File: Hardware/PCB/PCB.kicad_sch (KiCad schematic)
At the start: 0 parts

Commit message: added a lot of stuff, going to work on LCD + Touch next
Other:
- added sheet power (power.kicad_sch)
- added sheet relay_driver (relay_driver.kicad_sch)
- added sheet rtc (rtc.kicad_sch)
- added sheet serial_spi_lcd (serial_spi_lcd.kicad_sch)
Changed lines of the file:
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@@
 	(paper "A4")
 	(sheet
+		(at 36.83 154.94)
+		(size 19.685 13.97)
+		(fields_autoplaced yes)
+		(stroke
+			(width 0.1524)
+			(type solid)
+		)
+		(fill
+			(color 0 0 0 0.0000)
+		)
+		(property "Sheetname" "serial_spi_lcd"
+			(at 36.83 154.2284 0)
+			(effects
+				(font
+					(size 1.27 1.27)
+				)
+				(justify left bottom)
+			)
+		)
+		(property "Sheetfile" "serial_spi_lcd.kicad_sch"
+			(at 36.83 169.4946 0)
+			(effects
+				(font
+					(size 1.27 1.27)
+				)
+				(justify left top)
+			)
+		)
+		(instances
+			(project "PCB"
+				(path "/c3756407-a933-418d-a16a-ea4e5b091ef7"
+					(page "8")
+				)
+			)
+		)
+	)
+	(sheet
 		(at 209.55 102.87)
-		(size 35.56 24.13)
-		(fields_autoplaced yes)
-		(stroke
-			(width 0.1524)
-			(type solid)
-		)
-		(fill
-			(color 0 0 0 0.0000)
+		(size 26.67 29.845)
+		(fields_autoplaced yes)
+		(stroke
+			(width 0.1524)
+			(type solid)
+		)
+		(fill
+			(color 255 255 194 1.0000)
 		)
 		(property "Sheetname" "sensors"
@@
 		)
 		(property "Sheetfile" "sensors.kicad_sch"
-			(at 209.55 127.5846 0)
-			(effects
-				(font
-					(size 1.27 1.27)
-				)
-				(justify left top)
-			)
-		)
-		(instances
-			(project "PAC"
+			(at 209.55 133.2996 0)
+			(effects
+				(font
+					(size 1.27 1.27)
+				)
+				(justify left top)
+			)
+		)
+		(instances
+			(project "PCB"
 				(path "/c3756407-a933-418d-a16a-ea4e5b091ef7"
 					(page "3")
+				)
+			)
+		)
+	)
+	(sheet
+		(at 38.1 24.765)
+		(size 13.97 9.525)
+		(fields_autoplaced yes)
+		(stroke
+			(width 0.1524)
+			(type solid)
+		)
+		(fill
+			(color 72 72 72 1.0000)
+		)
+		(property "Sheetname" "power"
+			(at 38.1 24.0534 0)
+			(effects
+				(font
+					(size 1.27 1.27)
+				)
+				(justify left bottom)
+			)
+		)
+		(property "Sheetfile" "power.kicad_sch"
+			(at 38.1 34.8746 0)
+			(effects
+				(font
+					(size 1.27 1.27)
+				)
+				(justify left top)
+			)
+		)
+		(instances
+			(project "PCB"
+				(path "/c3756407-a933-418d-a16a-ea4e5b091ef7"
+					(page "5")
+				)
+			)
+		)
+	)
+	(sheet
+		(at 133.35 34.29)
+		(size 24.765 17.145)
+		(fields_autoplaced yes)
+		(stroke
+			(width 0.1524)
+			(type solid)
+		)
+		(fill
+			(color 255 255 194 1.0000)
+		)
+		(property "Sheetname" "relay_driver"
+			(at 133.35 33.5784 0)
+			(effects
+				(font
+					(size 1.27 1.27)
+				)
+				(justify left bottom)
+			)
+		)
+		(property "Sheetfile" "relay_driver.kicad_sch"
+			(at 133.35 52.0196 0)
+			(effects
+				(font
+					(size 1.27 1.27)
+				)
+				(justify left top)
+			)
+		)
+		(instances
+			(project "PCB"
+				(path "/c3756407-a933-418d-a16a-ea4e5b091ef7"
+					(page "6")
 				)
 			)
@@
 		)
 		(fill
-			(color 0 0 0 0.0000)
+			(color 255 255 194 1.0000)
 		)
 		(property "Sheetname" "motor_driver"
@@
 		)
 		(instances
-			(project "PAC"
+			(project "PCB"
 				(path "/c3756407-a933-418d-a16a-ea4e5b091ef7"
 					(page "2")
@@
 	)
 	(sheet
+		(at 28.575 89.535)
+		(size 19.05 18.415)
+		(fields_autoplaced yes)
+		(stroke
+			(width 0.1524)
+			(type solid)
+		)
+		(fill
+			(color 255 255 194 1.0000)
+		)
+		(property "Sheetname" "rtc"
+			(at 28.575 88.8234 0)
+			(effects
+				(font
+					(size 1.27 1.27)
+				)
+				(justify left bottom)
+			)
+		)
+		(property "Sheetfile" "rtc.kicad_sch"
+			(at 28.575 108.5346 0)
+			(effects
+				(font
+					(size 1.27 1.27)
+				)
+				(justify left top)
+			)
+		)
+		(instances
+			(project "PCB"
+				(path "/c3756407-a933-418d-a16a-ea4e5b091ef7"
+					(page "7")
+				)
+			)
+		)
+	)
+	(sheet
 		(at 91.44 57.15)
-		(size 26.67 26.67)
-		(fields_autoplaced yes)
-		(stroke
-			(width 0.1524)
-			(type solid)
-		)
-		(fill
-			(color 0 0 0 0.0000)
+		(size 21.59 65.405)
+		(fields_autoplaced yes)
+		(stroke
+			(width 0.1524)
+			(type solid)
+		)
+		(fill
+			(color 255 255 194 1.0000)
 		)
 		(property "Sheetname" "esp32"
@@
 		)
 		(property "Sheetfile" "esp32.kicad_sch"
-			(at 91.44 84.4046 0)
-			(effects
-				(font
-					(size 1.27 1.27)
-				)
-				(justify left top)
-			)
-		)
-		(instances
-			(project "PAC"
+			(at 91.44 123.1396 0)
+			(effects
+				(font
+					(size 1.27 1.27)
+				)
+				(justify left top)
+			)
+		)
+		(instances
+			(project "PCB"
 				(path "/c3756407-a933-418d-a16a-ea4e5b091ef7"
 					(page "4")

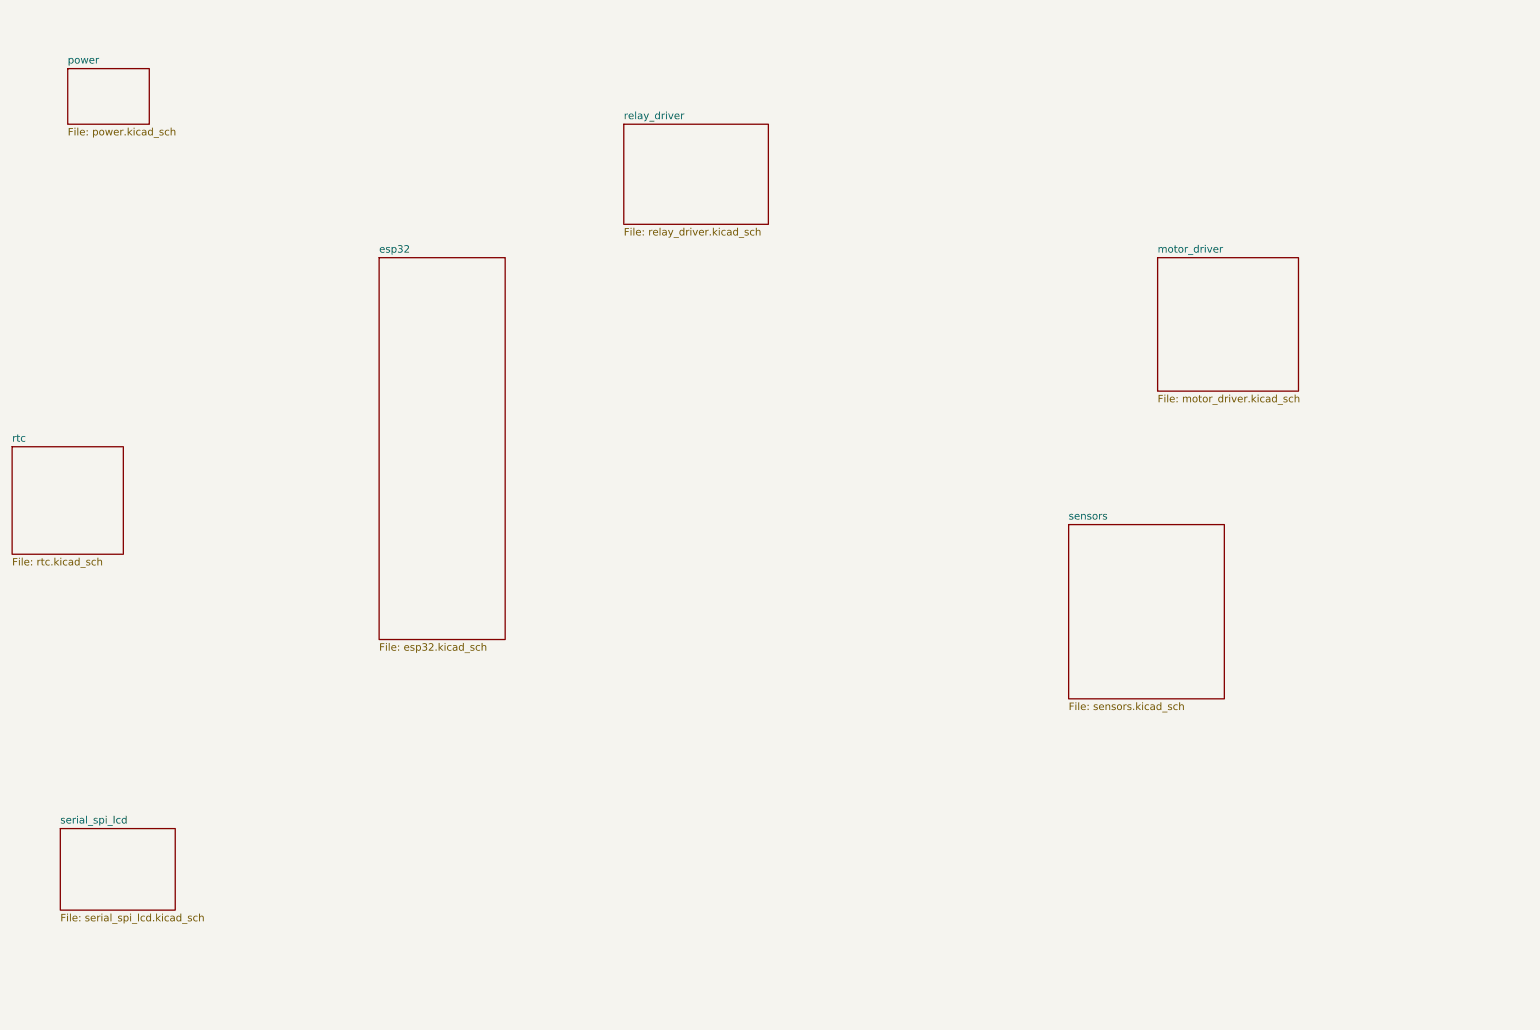
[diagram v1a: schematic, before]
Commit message: added symbol for LCD, working on adding PWM output terminal for brushless pump motors
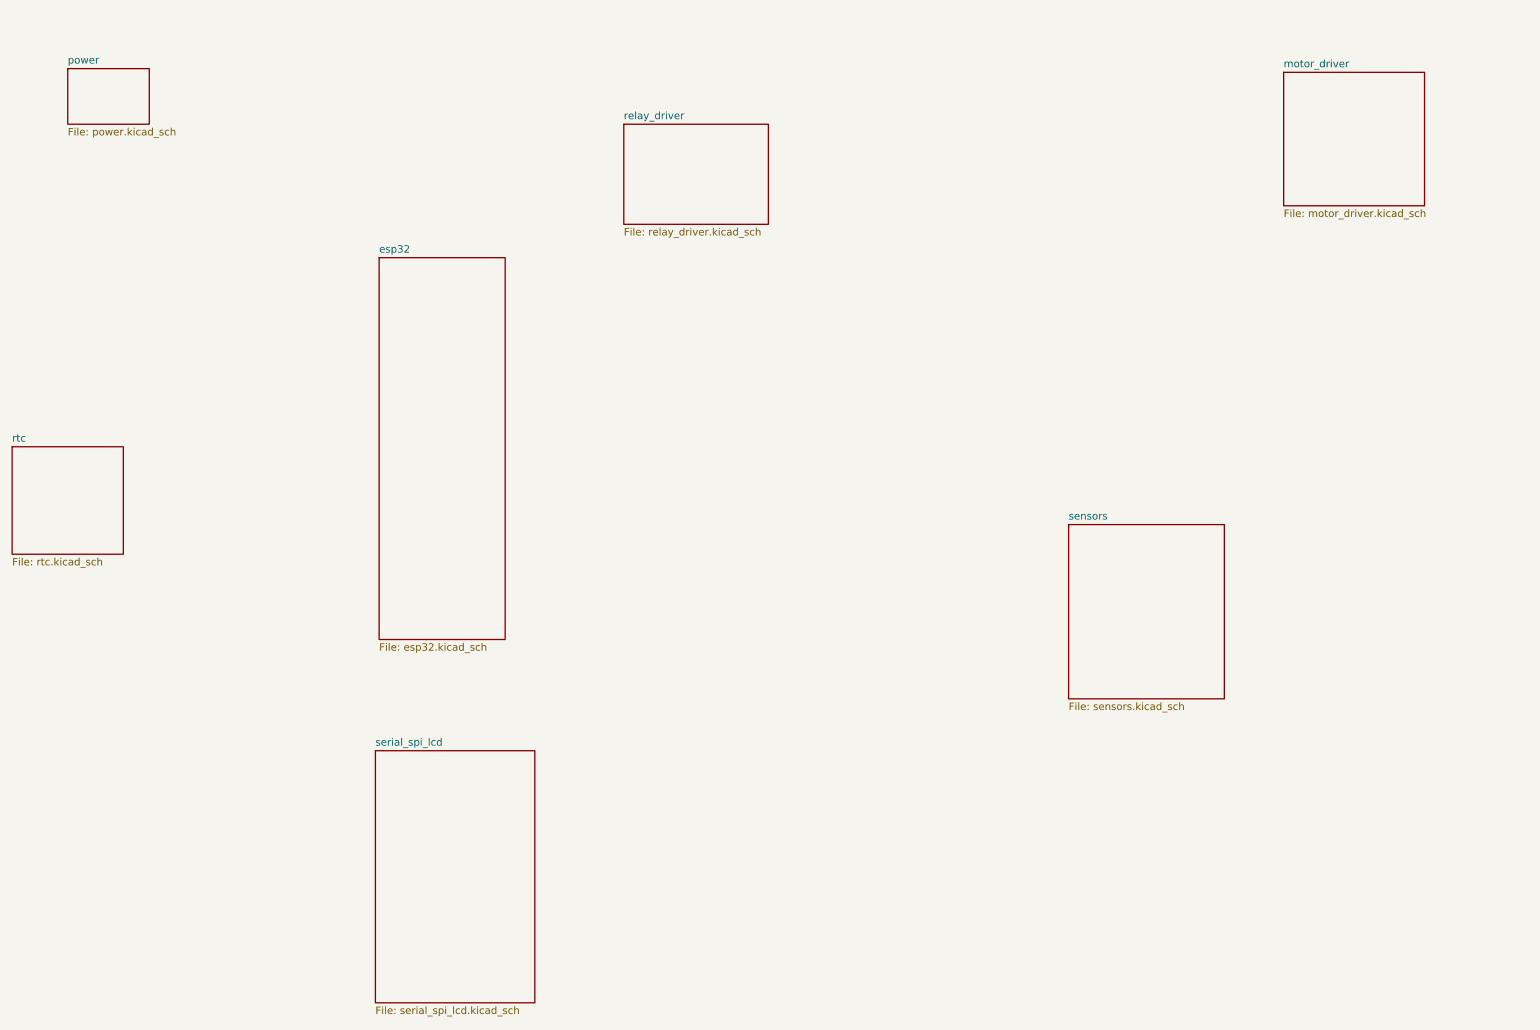
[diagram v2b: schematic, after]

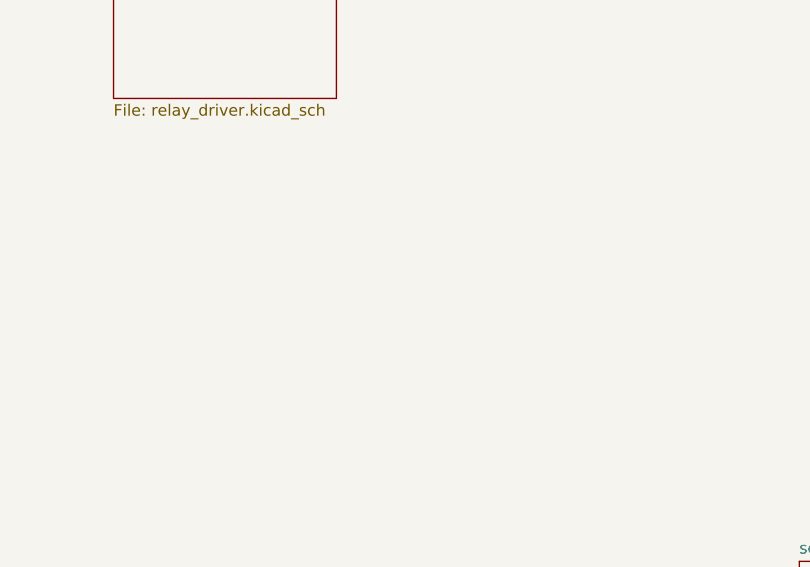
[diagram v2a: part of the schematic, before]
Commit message: switched to making buck converter to save costs and space, and to allow for LDO after 5.5V for better stability
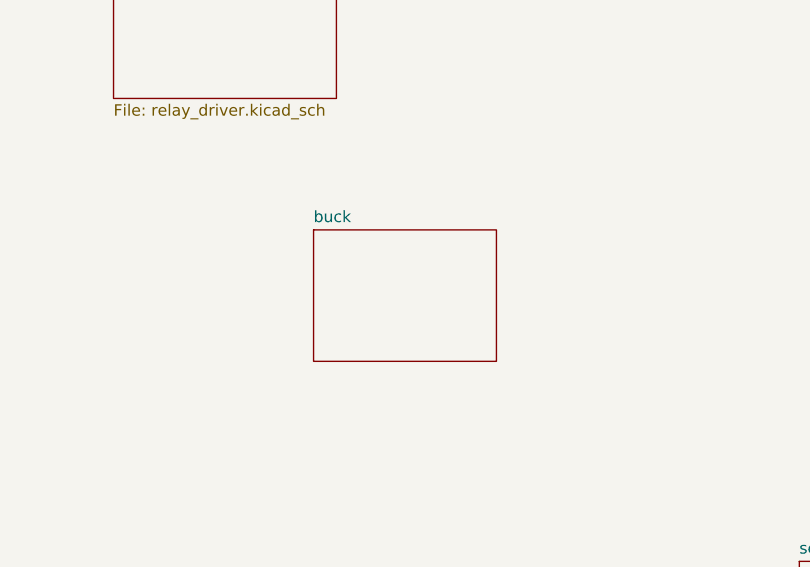
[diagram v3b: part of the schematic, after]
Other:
- added sheet buck (buck.kicad_sch)

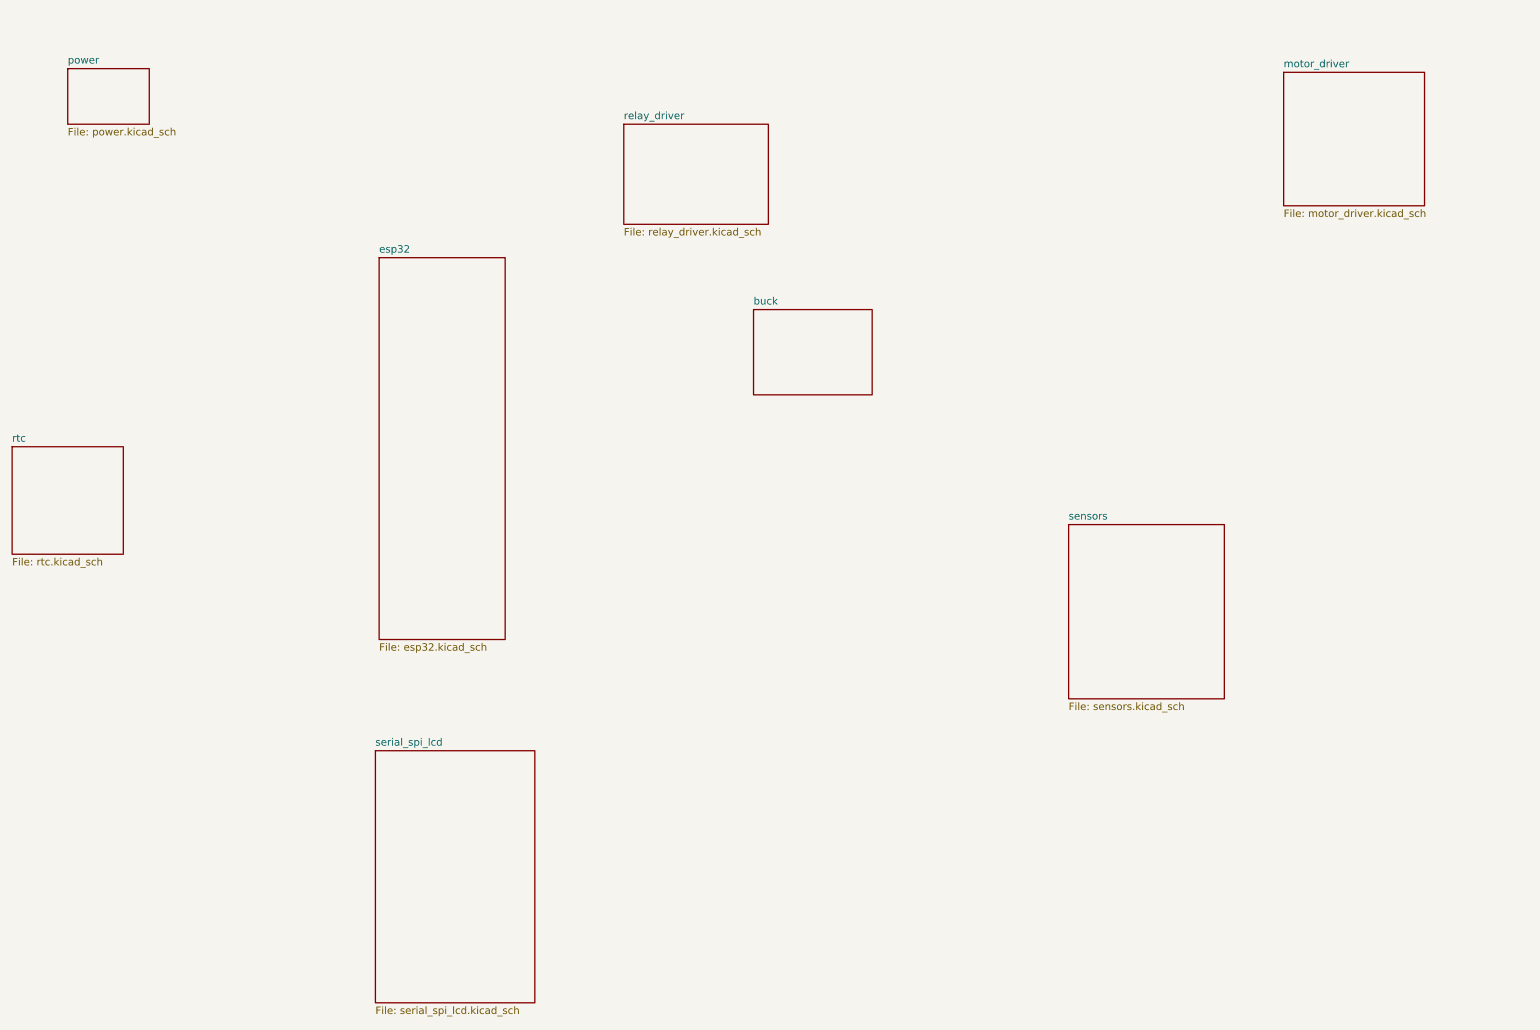
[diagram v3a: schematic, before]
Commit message: swapped to be better precision resistors for feedback on buck and votlage reference for ADCs
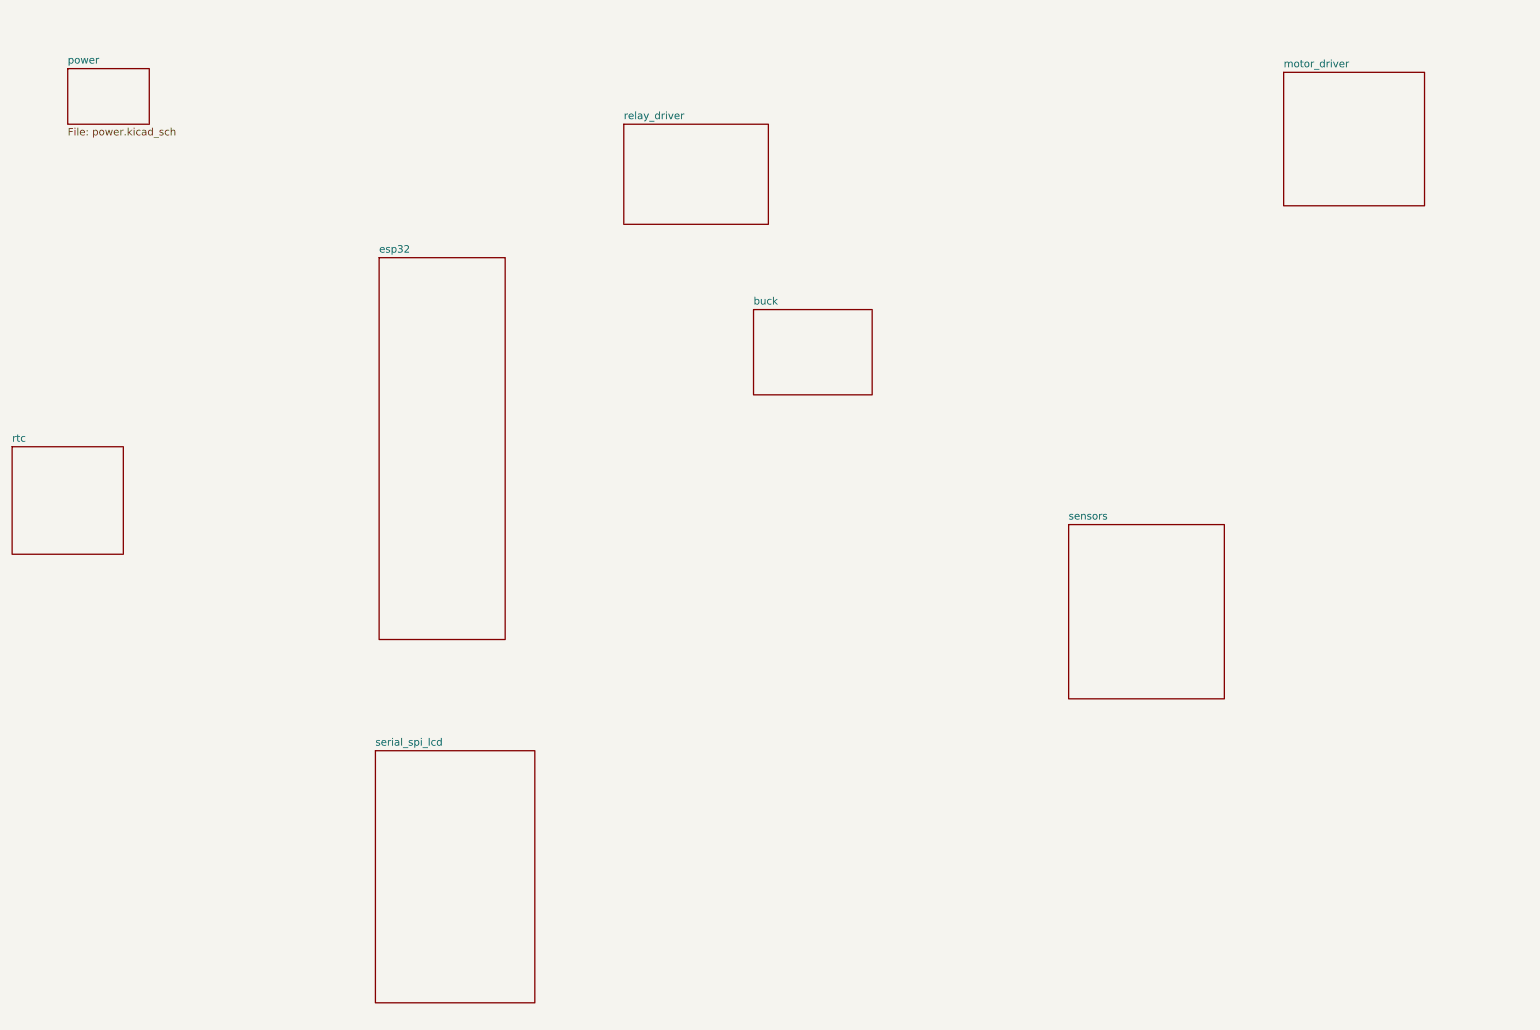
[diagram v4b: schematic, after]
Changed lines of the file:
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@@
 				)
 				(justify left top)
+				(hide yes)
 			)
 		)
@@
 				)
 				(justify left top)
+				(hide yes)
 			)
 		)
@@
 				)
 				(justify left top)
+				(hide yes)
 			)
 		)
@@
 				)
 				(justify left top)
+				(hide yes)
 			)
 		)
@@
 				)
 				(justify left top)
+				(hide yes)
 			)
 		)
@@
 				)
 				(justify left top)
-			)
-		)
+				(hide yes)
+			)
+		)
